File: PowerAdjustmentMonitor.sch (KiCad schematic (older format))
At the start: 44 parts, among them K2 CONN_3, K3 CONN_3, P6 CONN_1, P7 CONN_1, U3 LM317T, U4 LM317T, U5 LM337T, U6 LM337T

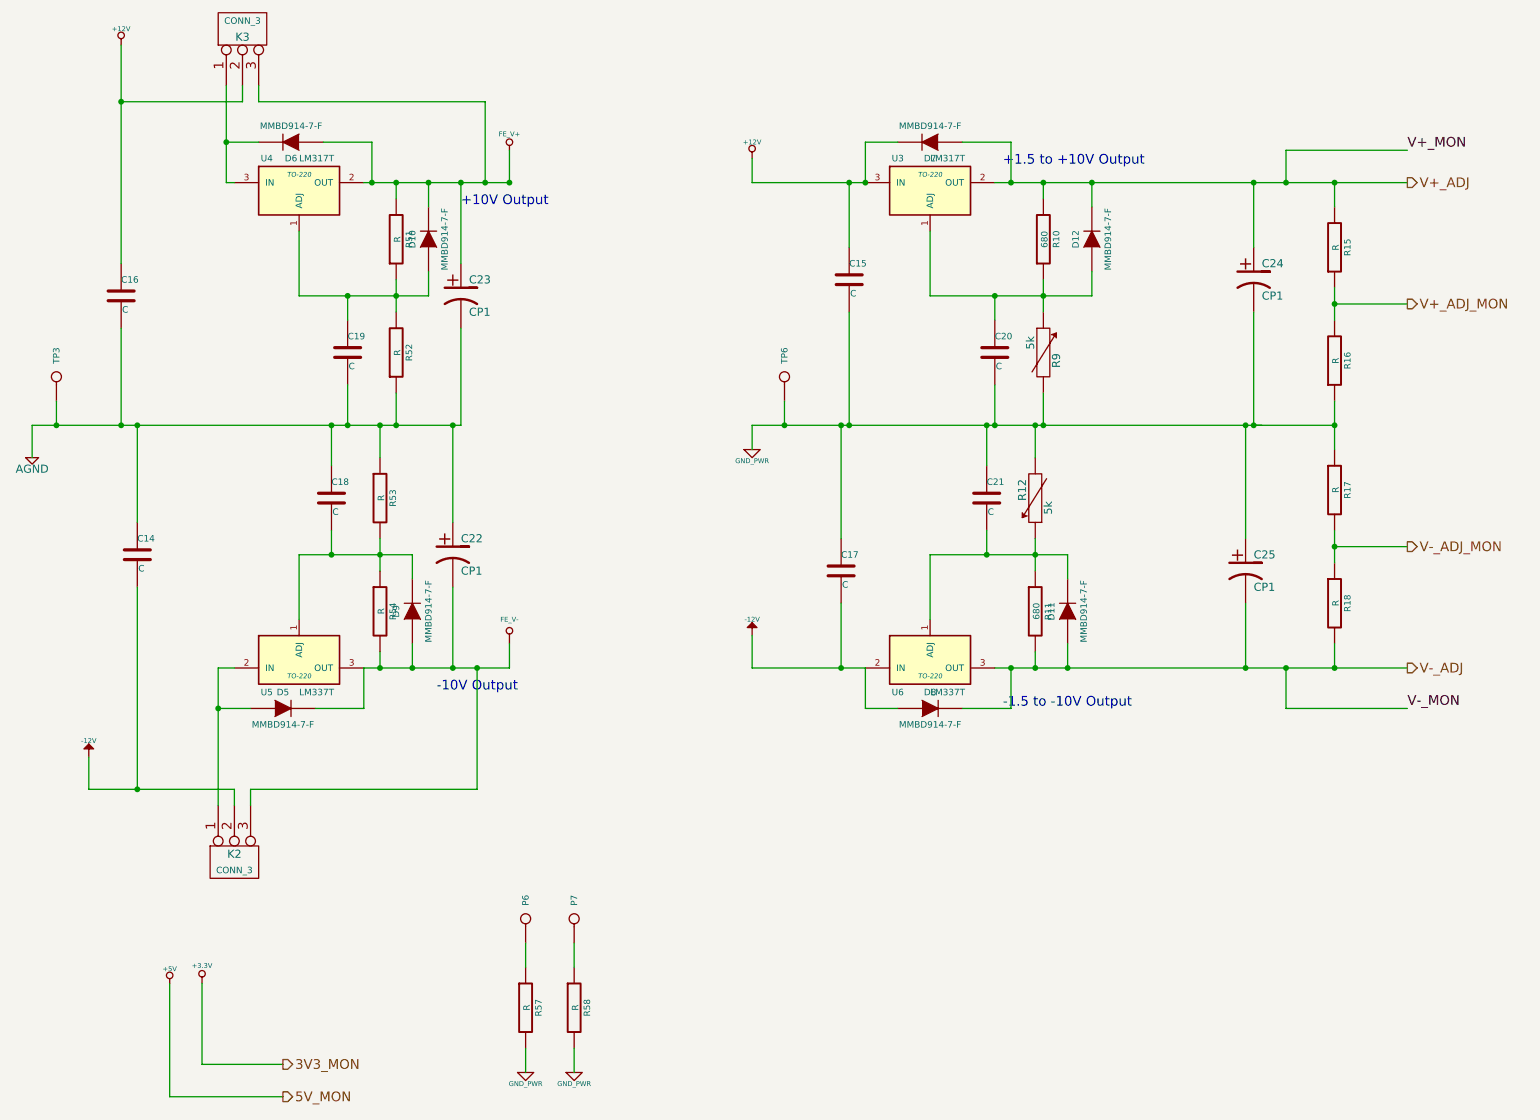
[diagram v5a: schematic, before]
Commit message: Assigned values to passives in Arduino, power adjustment monitor, relay and terminal block schematics
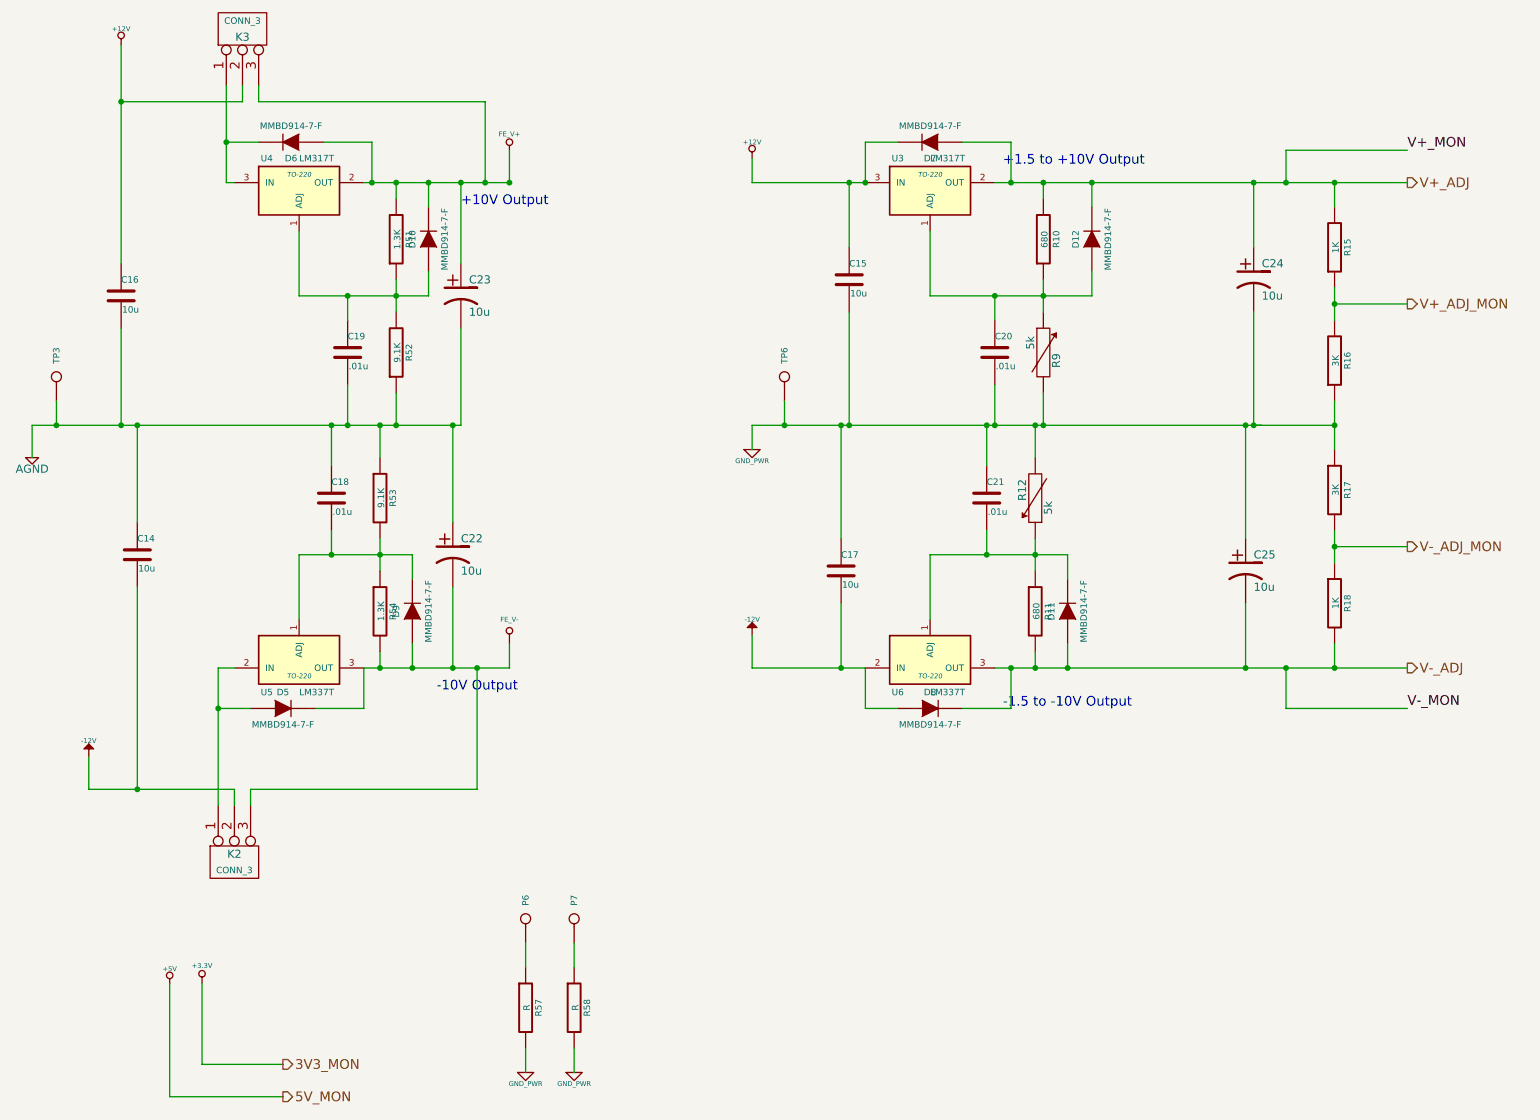
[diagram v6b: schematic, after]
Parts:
- C14, C15, C16, C17: value C -> 10u
- C18, C19, C20, C21: value C -> .01u
- C22, C23, C24, C25: value CP1 -> 10u
- R15, R18: value R -> 1K
- R16, R17: value R -> 3K
- R51, R54: value R -> 1.3K
- R52, R53: value R -> 9.1K
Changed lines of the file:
@@
 P 9200 2300
 F 0 "R15" V 9280 2300 40  0000 C CNN
-F 1 "R" V 9207 2301 40  0000 C CNN
+F 1 "1K" V 9207 2301 40  0000 C CNN
 F 2 "" V 9130 2300 30  0000 C CNN
 F 3 "" H 9200 2300 30  0000 C CNN
@@
 P 9200 3000
 F 0 "R16" V 9280 3000 40  0000 C CNN
-F 1 "R" V 9207 3001 40  0000 C CNN
+F 1 "3K" V 9207 3001 40  0000 C CNN
 F 2 "" V 9130 3000 30  0000 C CNN
 F 3 "" H 9200 3000 30  0000 C CNN
@@
 P 9200 4500
 F 0 "R18" V 9280 4500 40  0000 C CNN
-F 1 "R" V 9207 4501 40  0000 C CNN
+F 1 "1K" V 9207 4501 40  0000 C CNN
 F 2 "" V 9130 4500 30  0000 C CNN
 F 3 "" H 9200 4500 30  0000 C CNN
@@
 P 9200 3800
 F 0 "R17" V 9280 3800 40  0000 C CNN
-F 1 "R" V 9207 3801 40  0000 C CNN
+F 1 "3K" V 9207 3801 40  0000 C CNN
 F 2 "" V 9130 3800 30  0000 C CNN
 F 3 "" H 9200 3800 30  0000 C CNN
@@
 P 3400 2250
 F 0 "R51" V 3480 2250 40  0000 C CNN
-F 1 "R" V 3407 2251 40  0000 C CNN
+F 1 "1.3K" V 3407 2251 40  0000 C CNN
 F 2 "" V 3330 2250 30  0000 C CNN
 F 3 "" H 3400 2250 30  0000 C CNN
@@
 P 3400 2950
 F 0 "R52" V 3480 2950 40  0000 C CNN
-F 1 "R" V 3407 2951 40  0000 C CNN
+F 1 "9.1K" V 3407 2951 40  0000 C CNN
 F 2 "" V 3330 2950 30  0000 C CNN
 F 3 "" H 3400 2950 30  0000 C CNN
@@
 P 3300 4550
 F 0 "R54" V 3380 4550 40  0000 C CNN
-F 1 "R" V 3307 4551 40  0000 C CNN
+F 1 "1.3K" V 3307 4551 40  0000 C CNN
 F 2 "" V 3230 4550 30  0000 C CNN
 F 3 "" H 3300 4550 30  0000 C CNN
@@
 P 3300 3850
 F 0 "R53" V 3380 3850 40  0000 C CNN
-F 1 "R" V 3307 3851 40  0000 C CNN
+F 1 "9.1K" V 3307 3851 40  0000 C CNN
 F 2 "" V 3230 3850 30  0000 C CNN
 F 3 "" H 3300 3850 30  0000 C CNN
@@
 P 6150 4300
 F 0 "C17" H 6150 4400 40  0000 L CNN
-F 1 "C" H 6156 4215 40  0000 L CNN
+F 1 "10u" H 6156 4215 40  0000 L CNN
 F 2 "" H 6188 4150 30  0000 C CNN
 F 3 "" H 6150 4300 60  0000 C CNN
@@
 P 6200 2500
 F 0 "C15" H 6200 2600 40  0000 L CNN
-F 1 "C" H 6206 2415 40  0000 L CNN
+F 1 "10u" H 6206 2415 40  0000 L CNN
 F 2 "" H 6238 2350 30  0000 C CNN
 F 3 "" H 6200 2500 60  0000 C CNN
@@
 P 1800 4200
 F 0 "C14" H 1800 4300 40  0000 L CNN
-F 1 "C" H 1806 4115 40  0000 L CNN
+F 1 "10u" H 1806 4115 40  0000 L CNN
 F 2 "" H 1838 4050 30  0000 C CNN
 F 3 "" H 1800 4200 60  0000 C CNN
@@
 P 1700 2600
 F 0 "C16" H 1700 2700 40  0000 L CNN
-F 1 "C" H 1706 2515 40  0000 L CNN
+F 1 "10u" H 1706 2515 40  0000 L CNN
 F 2 "" H 1738 2450 30  0000 C CNN
 F 3 "" H 1700 2600 60  0000 C CNN
@@
 P 3100 2950
 F 0 "C19" H 3100 3050 40  0000 L CNN
-F 1 "C" H 3106 2865 40  0000 L CNN
+F 1 ".01u" H 3106 2865 40  0000 L CNN
 F 2 "" H 3138 2800 30  0000 C CNN
 F 3 "" H 3100 2950 60  0000 C CNN
@@
 P 3000 3850
 F 0 "C18" H 3000 3950 40  0000 L CNN
-F 1 "C" H 3006 3765 40  0000 L CNN
+F 1 ".01u" H 3006 3765 40  0000 L CNN
 F 2 "" H 3038 3700 30  0000 C CNN
 F 3 "" H 3000 3850 60  0000 C CNN
@@
 P 8700 2500
 F 0 "C24" H 8750 2600 50  0000 L CNN
-F 1 "CP1" H 8750 2400 50  0000 L CNN
+F 1 "10u" H 8750 2400 50  0000 L CNN
 F 2 "" H 8700 2500 60  0000 C CNN
 F 3 "" H 8700 2500 60  0000 C CNN
@@
 P 8650 4300
 F 0 "C25" H 8700 4400 50  0000 L CNN
-F 1 "CP1" H 8700 4200 50  0000 L CNN
+F 1 "10u" H 8700 4200 50  0000 L CNN
 F 2 "" H 8650 4300 60  0000 C CNN
 F 3 "" H 8650 4300 60  0000 C CNN
@@
 P 7100 2950
 F 0 "C20" H 7100 3050 40  0000 L CNN
-F 1 "C" H 7106 2865 40  0000 L CNN
+F 1 ".01u" H 7106 2865 40  0000 L CNN
 F 2 "" H 7138 2800 30  0000 C CNN
 F 3 "" H 7100 2950 60  0000 C CNN
@@
 P 7050 3850
 F 0 "C21" H 7050 3950 40  0000 L CNN
-F 1 "C" H 7056 3765 40  0000 L CNN
+F 1 ".01u" H 7056 3765 40  0000 L CNN
 F 2 "" H 7088 3700 30  0000 C CNN
 F 3 "" H 7050 3850 60  0000 C CNN
@@
 P 3750 4200
 F 0 "C22" H 3800 4300 50  0000 L CNN
-F 1 "CP1" H 3800 4100 50  0000 L CNN
+F 1 "10u" H 3800 4100 50  0000 L CNN
 F 2 "" H 3750 4200 60  0000 C CNN
 F 3 "" H 3750 4200 60  0000 C CNN
@@
 P 3800 2600
 F 0 "C23" H 3850 2700 50  0000 L CNN
-F 1 "CP1" H 3850 2500 50  0000 L CNN
+F 1 "10u" H 3850 2500 50  0000 L CNN
 F 2 "" H 3800 2600 60  0000 C CNN
 F 3 "" H 3800 2600 60  0000 C CNN

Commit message: Back-annotated footprints into the schematic
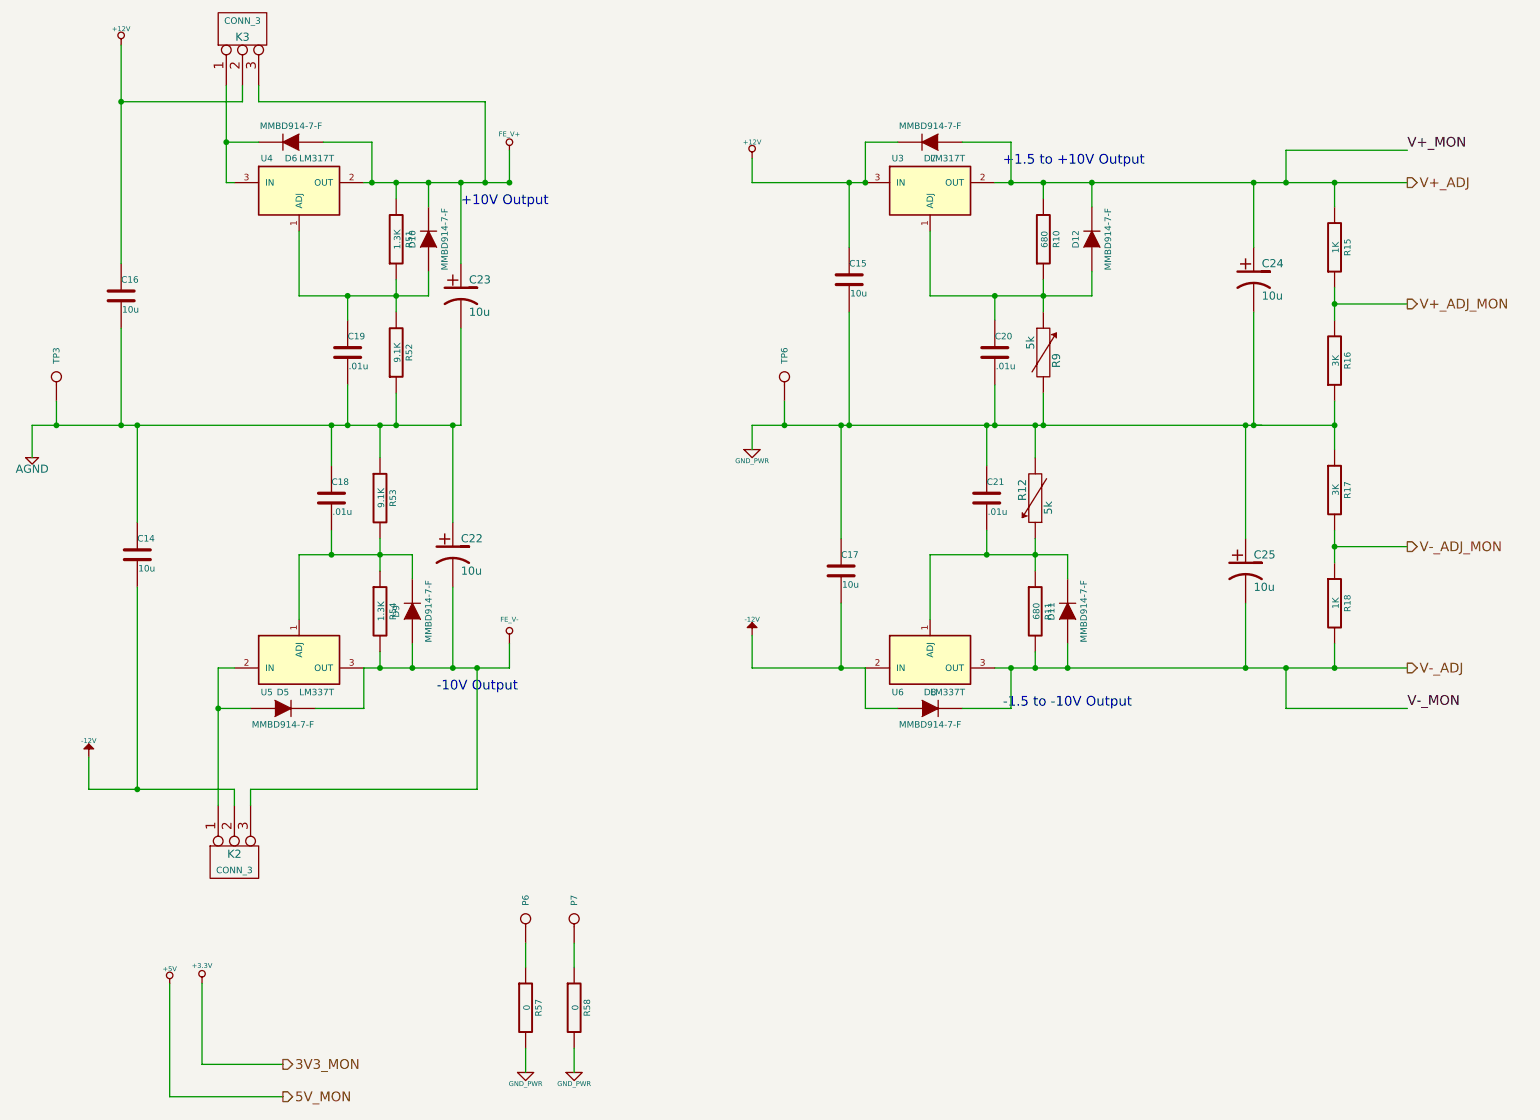
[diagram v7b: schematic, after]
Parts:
- C14, C15, C16, C17, C18, C19, C20, C21, C22, C23, C24, C25: footprint (none) -> Capacitors_SMD:c_0805
- D10, D11, D12, D5, D6, D7, D8, D9: footprint (none) -> BenchBudEE:SOT23-DIODE
- K2, K3: footprint (none) -> Pin_Headers:Pin_Header_Straight_1x03
- P6, P7: footprint (none) -> BenchBudEE:V8508H
- R10, R11, R15, R16, R17, R18, R51, R52, R53, R54: footprint (none) -> SMD_Packages:SM0805
- R12, R9: footprint (none) -> BenchBudEE:EVUE3K
- R57, R58: value R -> 0; footprint (none) -> SMD_Packages:SM0805
- TP3, TP6: footprint (none) -> BenchBudEE:TestPointTH
- U3, U4, U5, U6: footprint TO-220 -> Transistors_TO-220:TO-220_Neutral123_Vertical

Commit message: Final part numbers added to schematic, cross-checked KiCAD BOM against manual BOM
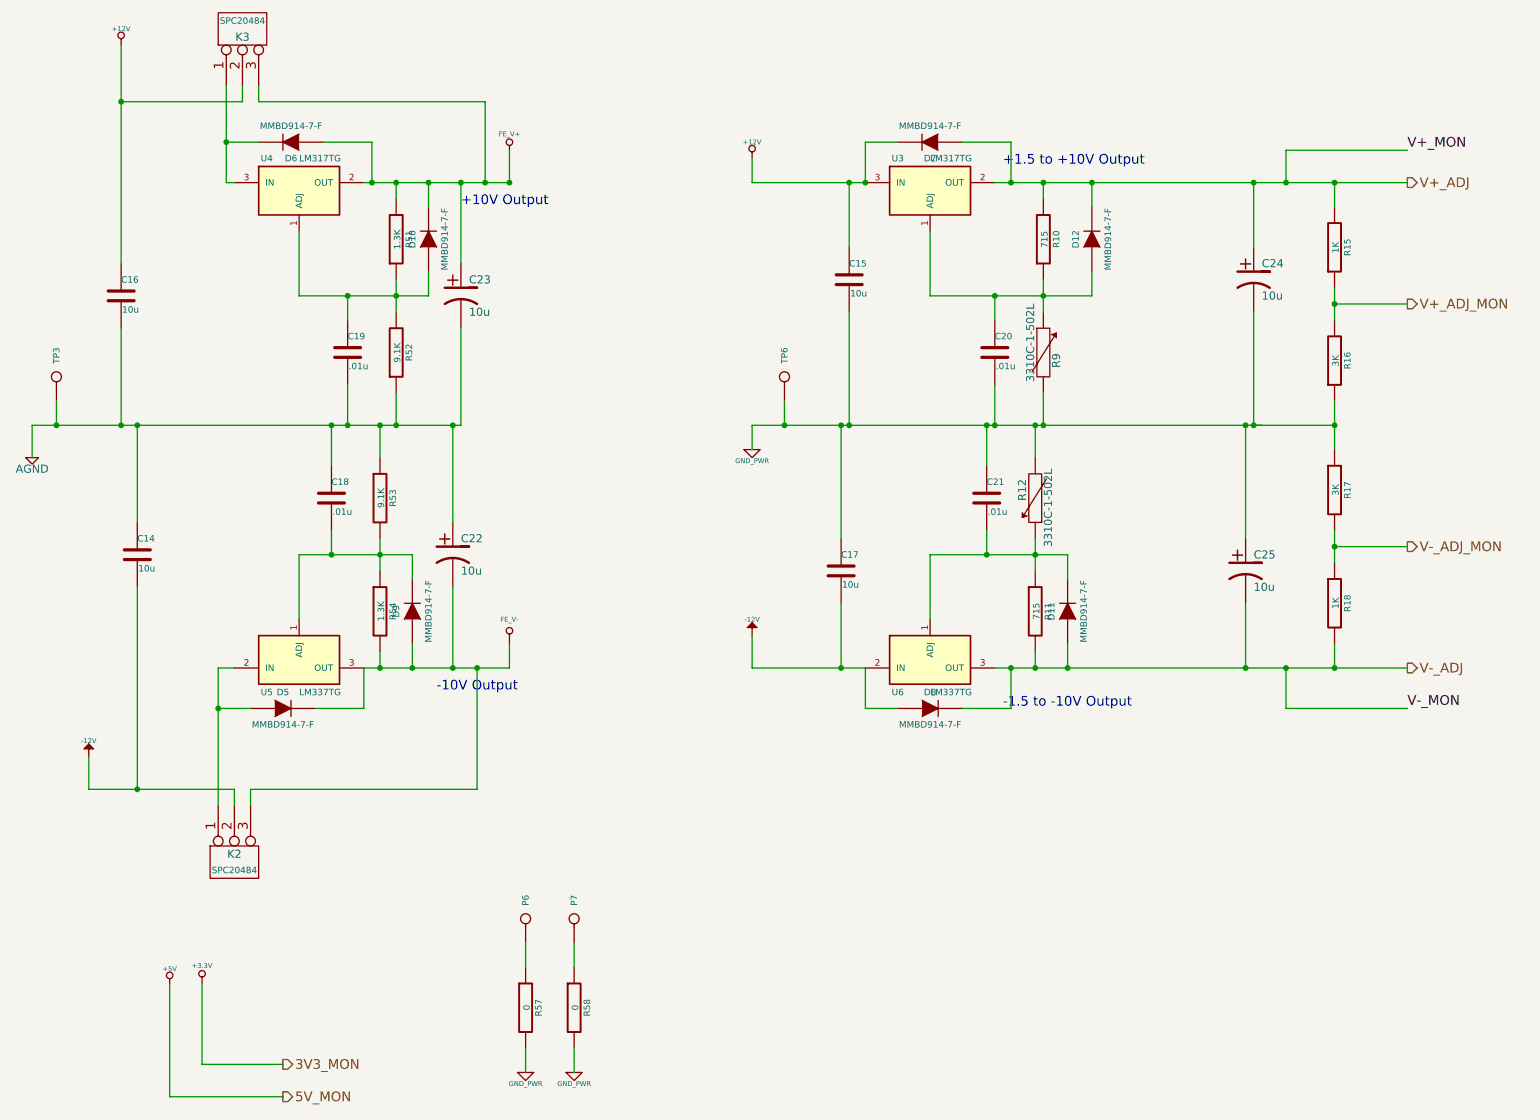
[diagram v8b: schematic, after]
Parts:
- K2, K3: value CONN_3 -> SPC20484
- P6, P7: value CONN_1 -> MC33282
- R10, R11: value 680 -> 715
- R12, R9: value 5k -> 3310C-1-502L
- U3, U4: value LM317T -> LM317TG
- U5, U6: value LM337T -> LM337TG
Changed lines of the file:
@@
 P 7350 4550
 F 0 "R11" V 7430 4550 40  0000 C CNN
-F 1 "680" V 7357 4551 40  0000 C CNN
+F 1 "715" V 7357 4551 40  0000 C CNN
 F 2 "SMD_Packages:SM0805" V 7280 4550 30  0001 C CNN
 F 3 "" H 7350 4550 30  0000 C CNN
@@
 P 6700 1950
 F 0 "U3" H 6500 2150 40  0000 C CNN
-F 1 "LM317T" H 6700 2150 40  0000 L CNN
+F 1 "LM317TG" H 6700 2150 40  0000 L CNN
 F 2 "Transistors_TO-220:TO-220_Neutral123_Vertical" H 6700 2050 30  0001 C CIN
 F 3 "" H 6700 1950 60  0000 C CNN
@@
 P 7400 2250
 F 0 "R10" V 7480 2250 40  0000 C CNN
-F 1 "680" V 7407 2251 40  0000 C CNN
+F 1 "715" V 7407 2251 40  0000 C CNN
 F 2 "SMD_Packages:SM0805" V 7330 2250 30  0001 C CNN
 F 3 "" H 7400 2250 30  0000 C CNN
@@
 P 7350 3850
 F 0 "R12" V 7430 3800 50  0000 C CNN
-F 1 "5k" V 7270 3910 50  0000 C CNN
+F 1 "3310C-1-502L" V 7270 3910 50  0000 C CNN
 F 2 "BenchBudEE:EVUE3K" H 7350 3850 60  0001 C CNN
 F 3 "" H 7350 3850 60  0000 C CNN
@@
 P 7400 2950
 F 0 "R9" V 7480 2900 50  0000 C CNN
-F 1 "5k" V 7320 3010 50  0000 C CNN
+F 1 "3310C-1-502L" V 7320 3010 50  0000 C CNN
 F 2 "BenchBudEE:EVUE3K" H 7400 2950 60  0001 C CNN
 F 3 "" H 7400 2950 60  0000 C CNN
@@
 P 2800 1950
 F 0 "U4" H 2600 2150 40  0000 C CNN
-F 1 "LM317T" H 2800 2150 40  0000 L CNN
+F 1 "LM317TG" H 2800 2150 40  0000 L CNN
 F 2 "Transistors_TO-220:TO-220_Neutral123_Vertical" H 2800 2050 30  0001 C CIN
 F 3 "" H 2800 1950 60  0000 C CNN
@@
 P 6700 4850
 F 0 "U6" H 6500 4650 40  0000 C CNN
-F 1 "LM337T" H 6700 4650 40  0000 L CNN
+F 1 "LM337TG" H 6700 4650 40  0000 L CNN
 F 2 "Transistors_TO-220:TO-220_Neutral123_Vertical" H 6700 4750 30  0001 C CIN
 F 3 "" H 6700 4850 60  0000 C CNN
@@
 P 2800 4850
 F 0 "U5" H 2600 4650 40  0000 C CNN
-F 1 "LM337T" H 2800 4650 40  0000 L CNN
+F 1 "LM337TG" H 2800 4650 40  0000 L CNN
 F 2 "Transistors_TO-220:TO-220_Neutral123_Vertical" H 2800 4750 30  0001 C CIN
 F 3 "" H 2800 4850 60  0000 C CNN
@@
 P 4200 6450
 F 0 "P6" H 4280 6450 40  0000 L CNN
-F 1 "CONN_1" H 4200 6505 30  0001 C CNN
+F 1 "MC33282" H 4200 6505 30  0001 C CNN
 F 2 "BenchBudEE:V8508H" H 4200 6450 60  0001 C CNN
 F 3 "" H 4200 6450 60  0000 C CNN
@@
 P 4500 6450
 F 0 "P7" H 4580 6450 40  0000 L CNN
-F 1 "CONN_1" H 4500 6505 30  0001 C CNN
+F 1 "MC33282" H 4500 6505 30  0001 C CNN
 F 2 "BenchBudEE:V8508H" H 4500 6450 60  0001 C CNN
 F 3 "" H 4500 6450 60  0000 C CNN
@@
 P 2450 950
 F 0 "K3" V 2400 950 50  0000 C CNN
-F 1 "CONN_3" V 2500 950 40  0000 C CNN
+F 1 "SPC20484" V 2500 950 40  0000 C CNN
 F 2 "Pin_Headers:Pin_Header_Straight_1x03" H 2450 950 60  0001 C CNN
 F 3 "" H 2450 950 60  0000 C CNN
@@
 P 2400 6100
 F 0 "K2" V 2350 6100 50  0000 C CNN
-F 1 "CONN_3" V 2450 6100 40  0000 C CNN
+F 1 "SPC20484" V 2450 6100 40  0000 C CNN
 F 2 "Pin_Headers:Pin_Header_Straight_1x03" H 2400 6100 60  0001 C CNN
 F 3 "" H 2400 6100 60  0000 C CNN
